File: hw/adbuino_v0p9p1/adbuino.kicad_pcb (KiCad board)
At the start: 2 copper layers, 25 x 50 mm, 74 parts, among them IC1 MAX3421EEHJ+, J1 Conn_01x06_Male, J2 U254-051N-4BH806, J3 USB_A, J4 Mini-DIN-4, J5 Mini-DIN-4, Q1 BSS138, Q2 BSS138, U1 AMS1117-3.3, U2 ATmega328P-AU, Y1 16MHz, Y2 12MHz

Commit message: updates
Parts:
- removed TP10, TP9: TestPoint_Small, TestPoint:TestPoint_Pad_D1.0mm
- moved JP6 44.2 mm to (52.7, 50.7), turned to 0 degrees
- moved TP15 43.0 mm to (61.6, 44.1), turned to 0 degrees
- moved TP17 41.6 mm to (61.6, 46.6), turned to 180 degrees
- moved TP3 38.3 mm to (60.5, 51.7), turned to 0 degrees
- moved JP3 38.2 mm to (54.4, 55.8)
- moved JP4 37.8 mm to (34.8, 54.0)
- moved TP5 37.3 mm to (60.3, 59.6), turned to 0 degrees
- moved TP16 36.5 mm to (37.5, 55.3)
- moved TP13 35.4 mm to (58.7, 53.2), turned to 180 degrees
- moved TP11 34.4 mm to (57.3, 50.2), turned to 180 degrees
- moved TP4 32.8 mm to (26.4, 56.1)
- moved TP7 30.8 mm to (28.1, 63.0)
- moved JP5 30.6 mm to (30.4, 53.9), turned to 90 degrees
- moved TP8 30.1 mm to (26.2, 64.3)
- moved TP12 29.6 mm to (44.9, 58.4)
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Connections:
- IC1 pad 15: SPI_MISO -> (no net)
- TP14 pad 1: SPI_MISO -> ATMEGA_SPI_MISO
- TP22 pad 1: (no net) -> ATMEGA_SPI_SCLK
- TP25 pad 1: (no net) -> ATMEGA_SPI_MOSI
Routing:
- net +3V3: track 0.00 -> 91.7 mm, vias 0 -> 4
- net ADB_1_5v: track 0.00 -> 34.3 mm, vias 0 -> 2
- net DEBUG_LED: track 0.00 -> 28.3 mm, vias 0 -> 2
- net ADB_1_DATA: track 0.00 -> 25.9 mm, vias 0 -> 3
- net ADB_1_PWR_ON: track 0.00 -> 25.8 mm, vias 0 -> 4
- net ATMEGA_SPI_SCLK: track 0.00 -> 24.8 mm, vias 0 -> 2
- net VBUS: track 0.00 -> 23.0 mm, vias 0 -> 1
- net ATMEGA_SPI_MISO: track 0.00 -> 23.0 mm, vias 0 -> 2
- net ATMEGA_SPI_MOSI: track 0.00 -> 19.0 mm, vias 0 -> 2
- net Host_USB_D+: track 0.00 -> 16.6 mm, vias 0 -> 2
- net Host_USB_D-: track 0.00 -> 15.5 mm, vias 0 -> 2
- net /RESET: track 0.00 -> 15.4 mm, vias 0 -> 3
- net Net-(C11-Pad1): track 0.00 -> 8.79 mm
- net VCC: track 0.00 -> 8.35 mm
- net Net-(D1-Pad2): track 0.00 -> 7.49 mm
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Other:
- rule trace_min: 0.2 -> 0.15

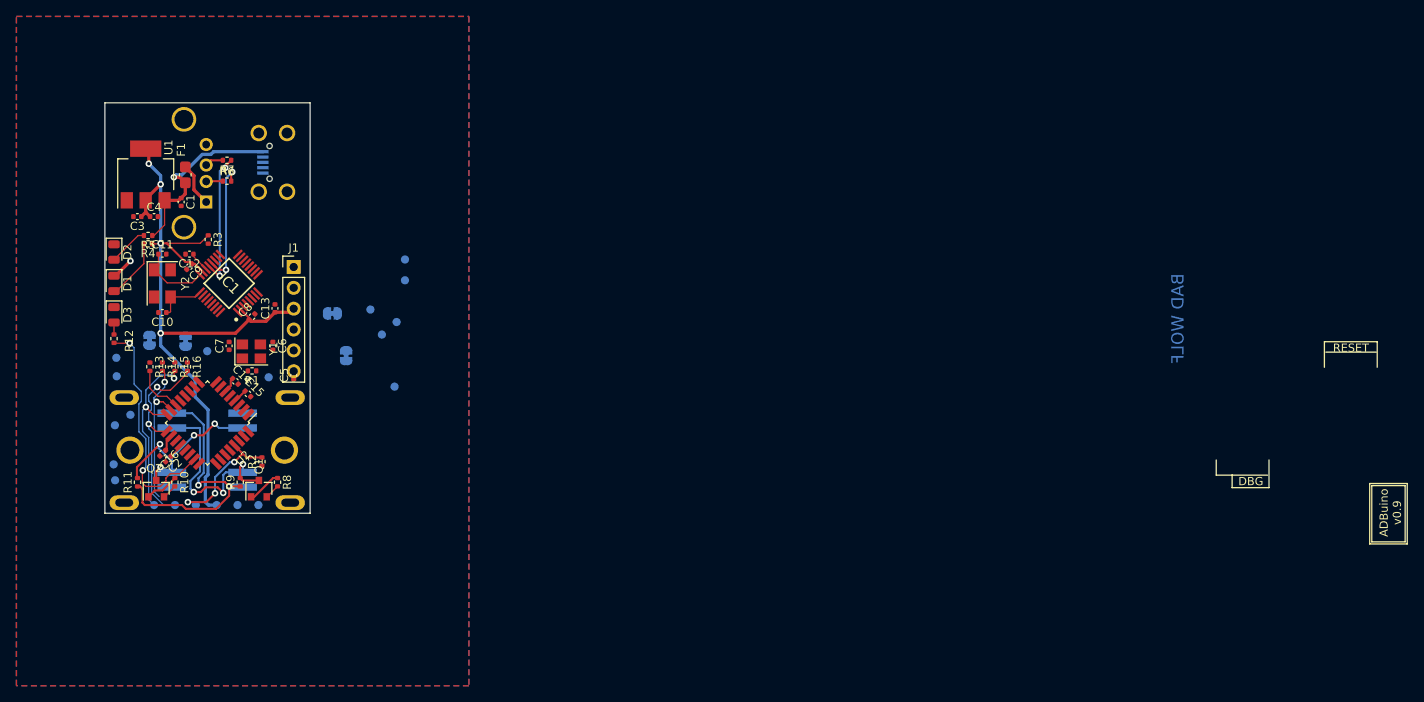
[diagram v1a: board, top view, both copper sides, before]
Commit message: First round of routing completed
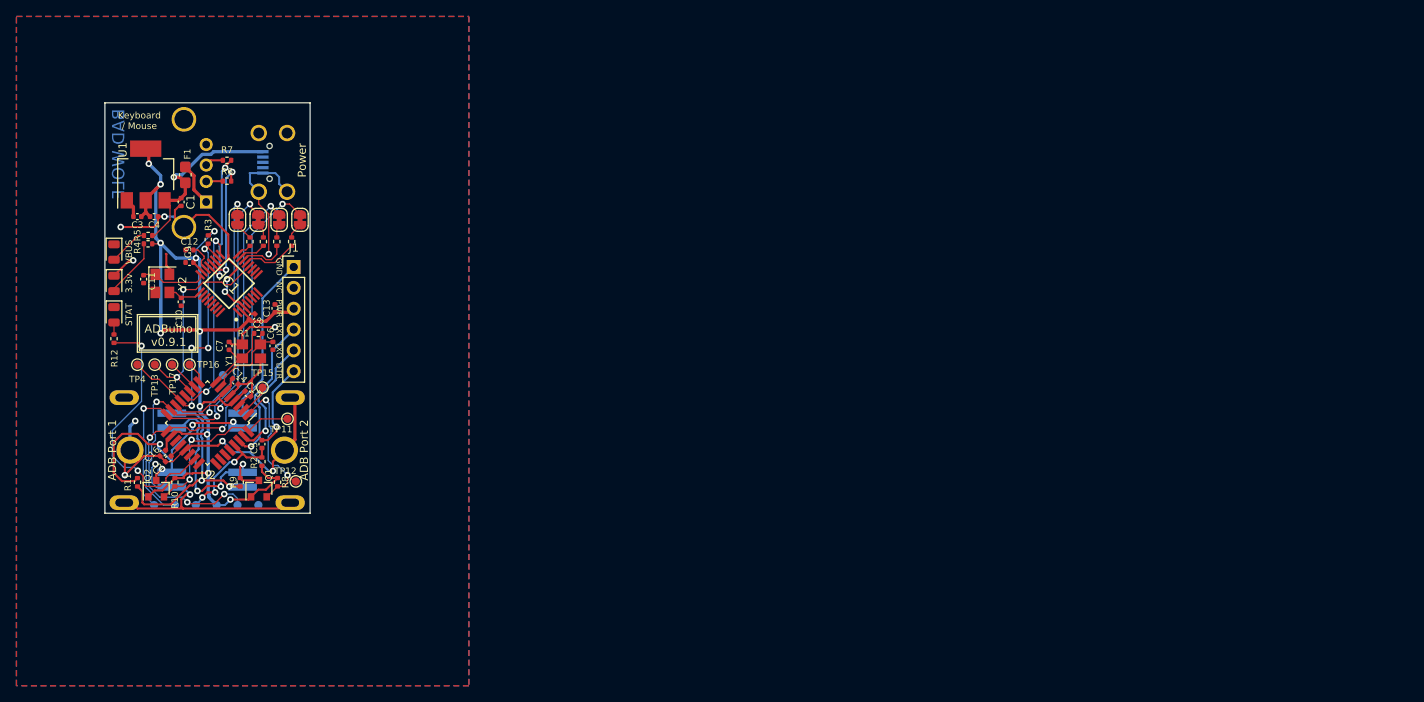
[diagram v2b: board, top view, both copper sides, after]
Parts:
- removed TP1, TP2, TP5, TP6, TP7, TP8: TestPoint_Small, TestPoint:TestPoint_Pad_D1.0mm
- JP3, JP4, JP5, JP6, TP11, TP12, TP13, TP15, TP16, TP17, TP4: moved to F.Cu
- R13, R14, R15, R16: value 500 -> 750
- Y2: footprint Crystal:Crystal_SMD_5032-4Pin_5.0x3.2mm -> Crystal:Crystal_SMD_3225-4Pin_3.2x2.5mm
- moved TP17 30.2 mm to (33.2, 56.9)
- moved TP13 27.9 mm to (31.1, 56.9)
- moved TP15 23.3 mm to (44.2, 59.7)
- moved TP3 22.1 mm to (39.4, 58.2)
- moved R13 21.7 mm to (45.9, 41.9), turned to 90 degrees
- moved JP5 21.6 mm to (46.2, 39.3), turned to 270 degrees
- moved JP4 20.3 mm to (48.8, 39.3)
- moved R16 19.8 mm to (47.8, 41.9), turned to 90 degrees
- moved JP3 19.7 mm to (43.7, 39.3)
- moved R15 18.7 mm to (44.3, 41.9), turned to 90 degrees
- moved R14 18.6 mm to (42.7, 41.9), turned to 90 degrees
- moved TP11 16.7 mm to (47.2, 63.5)
- moved JP6 16.2 mm to (41.1, 39.3), turned to 270 degrees
- moved TP12 13.1 mm to (48.3, 71.1), turned to 270 degrees
- moved C5 9.23 mm to (44.1, 66.6)
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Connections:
- IC1 pad 12: (no net) -> MAX3421_RESET
- IC1 pad 13: (no net) -> MAX3421_SPI_SCLK
- IC1 pad 15: (no net) -> MAX3421_SPI_MISO
- IC1 pad 16: (no net) -> MAX3421_SPI_MOSI
- J4 pad S1: Net-(J4-PadS1) -> GND
- J4 pad S2: Net-(J4-PadS1) -> GND
- J4 pad S3: Net-(J4-PadS1) -> GND
- J5 pad S1: Net-(J5-PadS1) -> GND
- J5 pad S2: Net-(J5-PadS1) -> GND
- J5 pad S3: Net-(J5-PadS1) -> GND
- JP3 pad 1: Net-(JP3-Pad1) -> ATMEGA_SPI_MISO
- JP3 pad 2: (no net) -> Net-(JP3-Pad2)
- JP4 pad 1: Net-(JP4-Pad1) -> ATMEGA_SPI_SCLK
- JP4 pad 2: (no net) -> Net-(JP4-Pad2)
- JP5 pad 1: Net-(JP5-Pad1) -> ATMEGA_SS
- JP5 pad 2: MAX3421_SS -> Net-(JP5-Pad2)
- JP6 pad 1: Net-(JP6-Pad1) -> ATMEGA_SPI_MOSI
- JP6 pad 2: (no net) -> Net-(JP6-Pad2)
- Q1 pad 1: VCC -> +3V3
- Q2 pad 1: VCC -> +3V3
- R10 pad 1: VCC -> +3V3
- R13 pad 1: Net-(JP5-Pad1) -> MAX3421_SS
- R13 pad 2: ATMEGA_SS -> Net-(JP5-Pad2)
- R14 pad 1: Net-(JP6-Pad1) -> MAX3421_SPI_MOSI
- R14 pad 2: ATMEGA_SPI_MOSI -> Net-(JP6-Pad2)
- R15 pad 1: Net-(JP3-Pad1) -> MAX3421_SPI_MISO
- R15 pad 2: ATMEGA_SPI_MISO -> Net-(JP3-Pad2)
- R16 pad 1: Net-(JP4-Pad1) -> MAX3421_SPI_SCLK
- R16 pad 2: ATMEGA_SPI_SCLK -> Net-(JP4-Pad2)
- R8 pad 1: VCC -> +3V3
- TP13 pad 1: TTL_MAX3421_RESET -> MAX3421_RESET
- U2 pad 11: TTL_MAX3421_RESET -> MAX3421_RESET
- U2 pad 19: Net-(TP1-Pad1) -> (no net)
- U2 pad 22: Net-(TP2-Pad1) -> (no net)
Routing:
- net GND: track 2.75 -> 171.7 mm, vias 1 -> 13
- net +3V3: track 91.7 -> 137.3 mm, vias 4 -> 11
- net ATMEGA_SPI_MOSI: track 19.0 -> 59.4 mm, vias 2 -> 5
- net MAX3421_INT: track 0.00 -> 33.0 mm, vias 0 -> 4
- net ATMEGA_SS: track 6.13 -> 34.9 mm, vias 0 -> 2
- net ATMEGA_SPI_MISO: track 23.0 -> 51.7 mm, vias 2 -> 3
- net ATMEGA_SPI_SCLK: track 24.8 -> 53.4 mm, vias 2 -> 3
- net MAX3421_RESET: track 0.00 -> 26.2 mm, vias 0 -> 2
- net MAX3421_GPX: track 0.00 -> 25.7 mm, vias 0 -> 2
- net ADB_PWR_ON_LV: track 1.85 -> 22.2 mm, vias 0 -> 2
- net FTDI_RXI: track 0.00 -> 18.6 mm, vias 0 -> 1
- net ADB_DATA_LV: track 1.85 -> 19.5 mm, vias 0 -> 2
- net FTDI_TXO: track 0.00 -> 15.3 mm, vias 0 -> 1
- net Net-(C6-Pad1): track 0.00 -> 11.2 mm
- net FTDI_DTR: track 0.00 -> 10.8 mm, vias 0 -> 1
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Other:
- board text added: "3.3v"
- board text added: "3v3"
- board text added: "ADB 1"
- board text added: "ADB 2"
- board text added: "ADBuino v0.9.1"
- board text added: "CLK"
- board text added: "Keyboard / Mouse"
- board text added: "MISO"
- board text added: "MOSI"
- board text added: "NC"
- board text added: "RST"
- board text added: "STAT"
- board text added: "USB Keyboard & Mouse"
- board text added: "VBUS"
- board text removed: "ADBuino v0.9"
- board text removed: "DBG"
- board text removed: "RESET"
- board text removed: "USB Keyboard / Mouse"
